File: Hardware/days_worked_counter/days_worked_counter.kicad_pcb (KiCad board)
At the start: 2 copper layers, 96.5 x 50 mm, 29 parts, among them J401 19V Input, SW201 RESET, U201 ATmega328P-A, U301 FT232RL, U401 LM1117-5.0, U501 SN74HC595, U601 SN74HC595, U701 SN74HC595

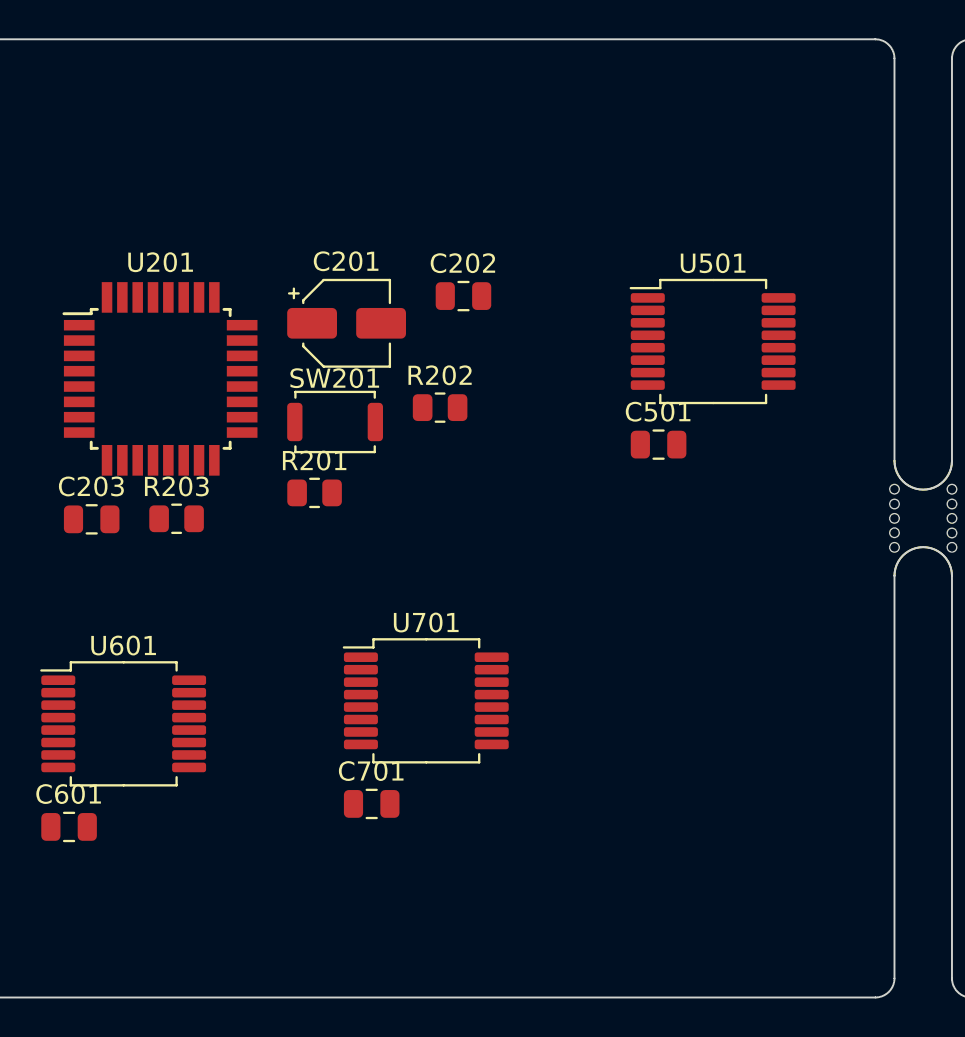
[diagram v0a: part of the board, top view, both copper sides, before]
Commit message: Add tidal force
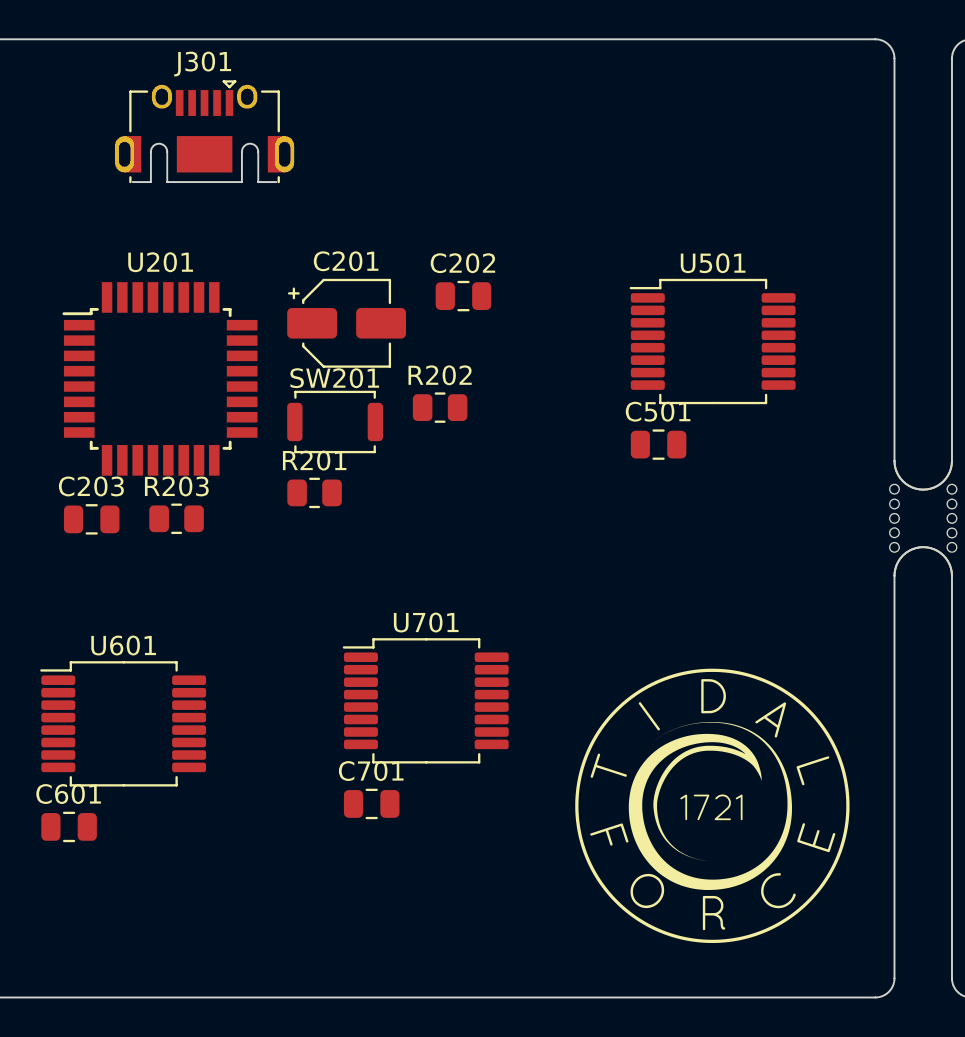
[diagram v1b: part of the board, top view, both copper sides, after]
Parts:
- added G***: LOGO, KenwoodFox:TIDAL_FORCE_LOGO, F.Cu at (188.0, 109.0)
- added J301: USB_B_Micro, Connector_USB:USB_Micro-AB_Molex_47590-0001, F.Cu at (161.5, 75.0)

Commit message: Cleanup more stuff
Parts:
- added Q501: MMBT3904, Package_TO_SOT_SMD:SOT-23, F.Cu at (138.0, 44.0)
- added Q601: MMBT3904, Package_TO_SOT_SMD:SOT-23, F.Cu at (125.6, 52.3)
- added Q701: MMBT3904, Package_TO_SOT_SMD:SOT-23, F.Cu at (125.6, 44.0)
- added R204: 1K, Resistor_SMD:R_0805_2012Metric, F.Cu at (137.8, 51.5)
- added R501: 10K, Resistor_SMD:R_0805_2012Metric, F.Cu at (142.7, 43.2)
- added R601: 10K, Resistor_SMD:R_0805_2012Metric, F.Cu at (130.2, 51.5)
- added R701: 10K, Resistor_SMD:R_0805_2012Metric, F.Cu at (130.2, 43.2)
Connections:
- U201 pad 12: unconnected-(U201-Pad12) -> /Display Card/DATA_IN
- U201 pad 13: unconnected-(U201-Pad13) -> /Display Card/CLOCK_IN
- U201 pad 14: unconnected-(U201-Pad14) -> /Display Card/LATCH_IN
- U201 pad 17: unconnected-(U201-Pad17) -> Net-(U201-Pad17)
- U201 pad 23: unconnected-(U201-Pad23) -> /MCU/DAY_RESET
- U201 pad 24: unconnected-(U201-Pad24) -> /MCU/DAY_ADVANCE
- U201 pad 25: unconnected-(U201-Pad25) -> /MCU/DAY_SUBTRACT
- U501 pad 15: unconnected-(U501-Pad15) -> /Display Card/SEG_A
- U601 pad 15: unconnected-(U601-Pad15) -> /Display Card1/SEG_A
- U701 pad 15: unconnected-(U701-Pad15) -> /Display Card2/SEG_A

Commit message: Add all the cool stuff
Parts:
- added Q502: MMBT3904, Package_TO_SOT_SMD:SOT-23, F.Cu at (191.5, 37.5)
- added Q503: MMBT3904, Package_TO_SOT_SMD:SOT-23, F.Cu at (191.5, 28.6)
- added Q504: MMBT3904, Package_TO_SOT_SMD:SOT-23, F.Cu at (196.4, 28.6)
- added Q505: MMBT3904, Package_TO_SOT_SMD:SOT-23, F.Cu at (186.6, 37.5)
- added Q506: MMBT3904, Package_TO_SOT_SMD:SOT-23, F.Cu at (186.6, 28.6)
- added Q507: MMBT3904, Package_TO_SOT_SMD:SOT-23, F.Cu at (186.6, 33.0)
- added Q508: MMBT3904, Package_TO_SOT_SMD:SOT-23, F.Cu at (191.5, 33.0)
- added Q602: MMBT3904, Package_TO_SOT_SMD:SOT-23, F.Cu at (158.7, 57.3)
- added Q603: MMBT3904, Package_TO_SOT_SMD:SOT-23, F.Cu at (158.7, 48.4)
- added Q604: MMBT3904, Package_TO_SOT_SMD:SOT-23, F.Cu at (163.6, 48.4)
- added Q605: MMBT3904, Package_TO_SOT_SMD:SOT-23, F.Cu at (153.8, 57.3)
- added Q606: MMBT3904, Package_TO_SOT_SMD:SOT-23, F.Cu at (153.8, 48.4)
- added Q607: MMBT3904, Package_TO_SOT_SMD:SOT-23, F.Cu at (153.8, 52.8)
- added Q608: MMBT3904, Package_TO_SOT_SMD:SOT-23, F.Cu at (158.7, 52.8)
- added Q702: MMBT3904, Package_TO_SOT_SMD:SOT-23, F.Cu at (158.7, 37.5)
- added Q703: MMBT3904, Package_TO_SOT_SMD:SOT-23, F.Cu at (158.7, 28.6)
- added Q704: MMBT3904, Package_TO_SOT_SMD:SOT-23, F.Cu at (163.6, 28.6)
- added Q705: MMBT3904, Package_TO_SOT_SMD:SOT-23, F.Cu at (153.8, 37.5)
- added Q706: MMBT3904, Package_TO_SOT_SMD:SOT-23, F.Cu at (153.8, 28.6)
- added Q707: MMBT3904, Package_TO_SOT_SMD:SOT-23, F.Cu at (153.8, 33.0)
- added Q708: MMBT3904, Package_TO_SOT_SMD:SOT-23, F.Cu at (158.7, 33.0)
- added R502: 10K, Resistor_SMD:R_0805_2012Metric, F.Cu at (205.0, 33.8)
- added R503: 10K, Resistor_SMD:R_0805_2012Metric, F.Cu at (200.6, 36.7)
- added R504: 10K, Resistor_SMD:R_0805_2012Metric, F.Cu at (196.2, 32.3)
- added R505: 10K, Resistor_SMD:R_0805_2012Metric, F.Cu at (195.2, 41.2)
- added R506: 750R?, Resistor_SMD:R_0805_2012Metric, F.Cu at (200.6, 33.8)
- added R507: 750R?, Resistor_SMD:R_0805_2012Metric, F.Cu at (205.4, 27.9)
- added R508: 750R?, Resistor_SMD:R_0805_2012Metric, F.Cu at (196.2, 35.2)
- added R509: 750R?, Resistor_SMD:R_0805_2012Metric, F.Cu at (205.4, 30.8)
- added R510: 10K, Resistor_SMD:R_0805_2012Metric, F.Cu at (201.0, 27.9)
- added R511: 10K, Resistor_SMD:R_0805_2012Metric, F.Cu at (190.8, 41.2)
- added R512: 10K, Resistor_SMD:R_0805_2012Metric, F.Cu at (199.6, 41.1)
- added R513: 750R?, Resistor_SMD:R_0805_2012Metric, F.Cu at (196.2, 38.2)
- added R514: 750R?, Resistor_SMD:R_0805_2012Metric, F.Cu at (209.9, 27.9)
- added R515: 750R?, Resistor_SMD:R_0805_2012Metric, F.Cu at (186.4, 41.2)
- added R516: 750R?, Resistor_SMD:R_0805_2012Metric, F.Cu at (201.0, 30.8)
- added R602: 10K, Resistor_SMD:R_0805_2012Metric, F.Cu at (172.2, 53.5)
- added R603: 10K, Resistor_SMD:R_0805_2012Metric, F.Cu at (167.7, 56.5)
- added R604: 10K, Resistor_SMD:R_0805_2012Metric, F.Cu at (163.3, 52.1)
- added R605: 10K, Resistor_SMD:R_0805_2012Metric, F.Cu at (162.4, 61.0)
- added R606: 750R?, Resistor_SMD:R_0805_2012Metric, F.Cu at (167.7, 53.5)
- added R607: 750R?, Resistor_SMD:R_0805_2012Metric, F.Cu at (172.6, 47.6)
- added R608: 750R?, Resistor_SMD:R_0805_2012Metric, F.Cu at (163.3, 55.0)
- added R609: 750R?, Resistor_SMD:R_0805_2012Metric, F.Cu at (172.6, 50.6)
- added R610: 10K, Resistor_SMD:R_0805_2012Metric, F.Cu at (168.2, 47.6)
- added R611: 10K, Resistor_SMD:R_0805_2012Metric, F.Cu at (158.0, 61.0)
- added R612: 10K, Resistor_SMD:R_0805_2012Metric, F.Cu at (166.8, 60.9)
- added R613: 750R?, Resistor_SMD:R_0805_2012Metric, F.Cu at (163.3, 58.0)
- added R614: 750R?, Resistor_SMD:R_0805_2012Metric, F.Cu at (177.0, 47.6)
- added R615: 750R?, Resistor_SMD:R_0805_2012Metric, F.Cu at (153.6, 61.0)
- added R616: 750R?, Resistor_SMD:R_0805_2012Metric, F.Cu at (168.2, 50.6)
- added R702: 10K, Resistor_SMD:R_0805_2012Metric, F.Cu at (172.2, 33.8)
- added R703: 10K, Resistor_SMD:R_0805_2012Metric, F.Cu at (167.7, 36.7)
- added R704: 10K, Resistor_SMD:R_0805_2012Metric, F.Cu at (163.3, 32.3)
- added R705: 10K, Resistor_SMD:R_0805_2012Metric, F.Cu at (162.4, 41.2)
- added R706: 750R?, Resistor_SMD:R_0805_2012Metric, F.Cu at (167.7, 33.8)
- added R707: 750R?, Resistor_SMD:R_0805_2012Metric, F.Cu at (172.6, 27.9)
- added R708: 750R?, Resistor_SMD:R_0805_2012Metric, F.Cu at (163.3, 35.2)
- added R709: 750R?, Resistor_SMD:R_0805_2012Metric, F.Cu at (172.6, 30.8)
- added R710: 10K, Resistor_SMD:R_0805_2012Metric, F.Cu at (168.2, 27.9)
- added R711: 10K, Resistor_SMD:R_0805_2012Metric, F.Cu at (158.0, 41.2)
- added R712: 10K, Resistor_SMD:R_0805_2012Metric, F.Cu at (166.8, 41.1)
- added R713: 750R?, Resistor_SMD:R_0805_2012Metric, F.Cu at (163.3, 38.2)
- added R714: 750R?, Resistor_SMD:R_0805_2012Metric, F.Cu at (177.0, 27.9)
- added R715: 750R?, Resistor_SMD:R_0805_2012Metric, F.Cu at (153.6, 41.2)
- added R716: 750R?, Resistor_SMD:R_0805_2012Metric, F.Cu at (168.2, 30.8)
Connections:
- net /Display Card/CLOCK_IN renamed /Display Card 0/CLOCK_IN
- net /Display Card/DATA_IN renamed /Display Card 0/DATA_IN
- net /Display Card/DATA_OUT renamed /Display Card 0/DATA_OUT
- net /Display Card/LATCH_IN renamed /Display Card 0/LATCH_IN
- net /Display Card1/DATA_OUT renamed /Display Card 1/DATA_OUT
- net /Display Card2/DATA_OUT renamed /Display Card 2/DATA_OUT
- Q501 pad 1: /Display Card/SEG_A -> /Display Card 0/SEG_B
- Q501 pad 3: /Display Card/SEG_A_LAMP -> Net-(Q501-Pad3)
- Q601 pad 1: /Display Card1/SEG_A -> /Display Card 1/SEG_B
- Q601 pad 3: /Display Card1/SEG_A_LAMP -> Net-(Q601-Pad3)
- Q701 pad 1: /Display Card2/SEG_A -> /Display Card 2/SEG_B
- Q701 pad 3: /Display Card2/SEG_A_LAMP -> Net-(Q701-Pad3)
- R501 pad 1: /Display Card/SEG_A -> /Display Card 0/SEG_B
- R601 pad 1: /Display Card1/SEG_A -> /Display Card 1/SEG_B
- R701 pad 1: /Display Card2/SEG_A -> /Display Card 2/SEG_B
- U501 pad 1: unconnected-(U501-Pad1) -> /Display Card 0/SEG_B
- U501 pad 15: /Display Card/SEG_A -> /Display Card 0/SEG_A
- U501 pad 2: unconnected-(U501-Pad2) -> /Display Card 0/SEG_C
- U501 pad 3: unconnected-(U501-Pad3) -> /Display Card 0/SEG_D
- U501 pad 4: unconnected-(U501-Pad4) -> /Display Card 0/SEG_E
- U501 pad 5: unconnected-(U501-Pad5) -> /Display Card 0/SEG_F
- U501 pad 6: unconnected-(U501-Pad6) -> /Display Card 0/SEG_G
- U501 pad 7: unconnected-(U501-Pad7) -> /Display Card 0/SEG_H
- U601 pad 1: unconnected-(U601-Pad1) -> /Display Card 1/SEG_B
- U601 pad 15: /Display Card1/SEG_A -> /Display Card 1/SEG_A
- U601 pad 2: unconnected-(U601-Pad2) -> /Display Card 1/SEG_C
- U601 pad 3: unconnected-(U601-Pad3) -> /Display Card 1/SEG_D
- U601 pad 4: unconnected-(U601-Pad4) -> /Display Card 1/SEG_E
- U601 pad 5: unconnected-(U601-Pad5) -> /Display Card 1/SEG_F
- U601 pad 6: unconnected-(U601-Pad6) -> /Display Card 1/SEG_G
- U601 pad 7: unconnected-(U601-Pad7) -> /Display Card 1/SEG_H
- U701 pad 1: unconnected-(U701-Pad1) -> /Display Card 2/SEG_B
- U701 pad 15: /Display Card2/SEG_A -> /Display Card 2/SEG_A
- U701 pad 2: unconnected-(U701-Pad2) -> /Display Card 2/SEG_C
- U701 pad 3: unconnected-(U701-Pad3) -> /Display Card 2/SEG_D
- U701 pad 4: unconnected-(U701-Pad4) -> /Display Card 2/SEG_E
- U701 pad 5: unconnected-(U701-Pad5) -> /Display Card 2/SEG_F
- U701 pad 6: unconnected-(U701-Pad6) -> /Display Card 2/SEG_G
- U701 pad 7: unconnected-(U701-Pad7) -> /Display Card 2/SEG_H

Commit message: Even more stuff
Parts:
- added BT201: 3v, Battery:BatteryHolder_Keystone_3034_1x20mm, F.Cu at (242.6, 114.6)
- added D201: STAT, LED_SMD:LED_0805_2012Metric, F.Cu at (215.0, 71.6)
- added J302: PROG, Connector_PinSocket_2.54mm:PinSocket_1x06_P2.54mm_Vertical, F.Cu at (88.7, 80.2)
- added J501: Conn_01x09, Connector_PinSocket_2.54mm:PinSocket_1x09_P2.54mm_Vertical, F.Cu at (269.6, 40.7)
- added J502: Conn_01x09, Connector_PinSocket_2.54mm:PinSocket_1x09_P2.54mm_Vertical, F.Cu at (274.2, 40.7)
- added J601: Conn_01x09, Connector_PinSocket_2.54mm:PinSocket_1x09_P2.54mm_Vertical, F.Cu at (242.3, 40.7)
- added J602: Conn_01x09, Connector_PinSocket_2.54mm:PinSocket_1x09_P2.54mm_Vertical, F.Cu at (246.9, 40.7)
- added J701: Conn_01x09, Connector_PinSocket_2.54mm:PinSocket_1x09_P2.54mm_Vertical, F.Cu at (215.1, 40.7)
- added J702: Conn_01x09, Connector_PinSocket_2.54mm:PinSocket_1x09_P2.54mm_Vertical, F.Cu at (219.7, 40.7)
- added JP301: SolderJumper_2_Open, Jumper:SolderJumper-2_P1.3mm_Open_TrianglePad1.0x1.5mm, F.Cu at (92.7, 87.8)
- added R205: 10K, Resistor_SMD:R_0805_2012Metric, F.Cu at (232.4, 127.1)
- added R206: 10K, Resistor_SMD:R_0805_2012Metric, F.Cu at (257.2, 111.5)
- added U202: DS1307Z+, Package_SO:SOIC-8_3.9x4.9mm_P1.27mm, F.Cu at (259.2, 106.8)
- J301: footprint Connector_USB:USB_Micro-AB_Molex_47590-0001 -> Connector_USB:USB_Mini-B_Lumberg_2486_01_Horizontal
- moved J301 84.0 mm to (77.6, 71.2), turned to 180 degrees
- moved R302 72.5 mm to (73.0, 98.0)
- moved D302 69.6 mm to (76.6, 98.0)
- moved D301 64.1 mm to (76.8, 94.0)
- moved U401 63.7 mm to (75.8, 120.6)
- moved R301 62.8 mm to (73.0, 94.0)
- moved D401 61.9 mm to (85.7, 121.2)
- moved C401 60.8 mm to (75.8, 125.4)
- moved J401 60.2 mm to (72.2, 130.2)
- moved C303 55.5 mm to (79.2, 77.2), turned to -90 degrees
- moved C301 53.4 mm to (70.2, 83.4), turned to -90 degrees
- moved R401 53.1 mm to (82.2, 121.2)
- moved C302 53.0 mm to (83.6, 77.6)
- moved U301 49.3 mm to (76.2, 85.4), turned to 180 degrees
- moved C304 43.1 mm to (84.2, 89.0), turned to 180 degrees
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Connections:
- U201 pad 27: unconnected-(U201-Pad27) -> /MCU/SDA
- U201 pad 28: unconnected-(U201-Pad28) -> /MCU/SCL

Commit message: get input from @ka2qfx
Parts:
- removed Q502, Q503, Q504, Q505, Q506, Q507, Q508, Q602, Q603, Q604, Q605, Q606, Q607, Q608, Q702, Q703, Q704, Q705, Q706, Q707, Q708: MMBT3904, Package_TO_SOT_SMD:SOT-23
- removed R502, R503, R504, R505, R510, R511, R512, R602, R603, R604, R605, R610, R611, R612, R702, R703, R704, R705, R710, R711, R712: 10K, Resistor_SMD:R_0805_2012Metric
- removed R506, R507, R508, R509, R513, R514, R515, R516, R606, R607, R608, R609, R613, R614, R615, R616, R706, R707, R708, R709, R713, R714, R715, R716: 750R?, Resistor_SMD:R_0805_2012Metric
- removed the mouse-bite-3mm-slot at (199.0, 94.0)
- added C204: 22pf, Capacitor_SMD:C_0805_2012Metric, F.Cu at (320.0, -7.20)
- added C205: 22pf, Capacitor_SMD:C_0805_2012Metric, F.Cu at (320.0, -10.2)
- added J101: OUT, Connector_PinSocket_2.54mm:PinSocket_1x06_P2.54mm_Vertical, F.Cu at (83.5, 127.2)
- added J102: IN, Connector_PinSocket_2.54mm:PinSocket_1x06_P2.54mm_Vertical, F.Cu at (91.5, 127.2)
- added J103: OUT, Connector_PinSocket_2.54mm:PinSocket_1x06_P2.54mm_Vertical, F.Cu at (118.5, 127.2)
- added J104: IN, Connector_PinSocket_2.54mm:PinSocket_1x06_P2.54mm_Vertical, F.Cu at (126.5, 127.2)
- added J105: OUT, Connector_PinSocket_2.54mm:PinSocket_1x06_P2.54mm_Vertical, F.Cu at (153.0, 127.2)
- added R207: 10K, Resistor_SMD:R_0805_2012Metric, F.Cu at (279.4, -17.8)
- added R208: 10K, Resistor_SMD:R_0805_2012Metric, F.Cu at (279.4, -20.8)
- added R209: 10K, Resistor_SMD:R_0805_2012Metric, F.Cu at (289.9, -29.3)
- added SW202: DAY_RESET, Button_Switch_THT:SW_PUSH_6mm_H5mm, F.Cu at (279.2, -28.8)
- added SW203: DAY_ADV, Button_Switch_THT:SW_PUSH_6mm_H5mm, F.Cu at (268.7, -28.8)
- added SW204: DAY_SUB, Button_Switch_THT:SW_PUSH_6mm_H5mm, F.Cu at (268.7, -20.2)
- added Y201: 16mHz, Crystal:Crystal_SMD_HC49-SD, F.Cu at (310.4, -8.59)
- added Y202: 32.768kHz, Crystal:Crystal_SMD_HC49-SD, F.Cu at (310.4, -2.34)
- added mouse-bite-3mm-slot: VAL**, Panelization:mouse-bite-3mm-slot, F.Cu at (122.5, 42.5)
- added mouse-bite-3mm-slot: VAL**, Panelization:mouse-bite-3mm-slot, F.Cu at (122.5, 147.5)
- added mouse-bite-3mm-slot: VAL**, Panelization:mouse-bite-3mm-slot, F.Cu at (87.5, 42.5)
- added mouse-bite-3mm-slot: VAL**, Panelization:mouse-bite-3mm-slot, F.Cu at (87.5, 147.5)
- J501, J601, J701: value Conn_01x09 -> Top Conn; moved to B.Cu
- J502, J602, J702: value Conn_01x09 -> Bottom Conn; moved to B.Cu
- SW201: footprint Button_Switch_SMD:SW_Push_SPST_NO_Alps_SKRK -> Button_Switch_THT:SW_PUSH_6mm_H5mm
- moved C301 272.4 mm to (266.2, -105.8)
- moved C302 272.4 mm to (279.6, -111.6)
- moved C303 272.4 mm to (275.2, -112.0)
- moved C304 272.4 mm to (280.2, -100.2)
- moved D301 272.4 mm to (272.8, -95.2)
- moved D302 272.4 mm to (272.6, -91.2)
- moved J301 272.4 mm to (273.6, -118.0)
- moved J302 272.4 mm to (284.7, -109.0)
- moved JP301 272.4 mm to (288.7, -101.4)
- moved Q501 272.4 mm to (334.0, -145.2)
- moved Q601 272.4 mm to (321.6, -136.9)
- moved Q701 272.4 mm to (321.6, -145.2)
- moved R204 272.4 mm to (333.8, -137.7)
- moved R301 272.4 mm to (269.0, -95.2)
- moved R302 272.4 mm to (269.0, -91.2)
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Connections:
- net Net-(J401-Pad1) renamed +19V
- J501 pad 1: /Display Card 0/SEG_E_LAMP -> /Display Card 0/SEG_B_LAMP
- J501 pad 3: /Display Card 0/SEG_F_LAMP -> /Display Card 0/SEG_A_LAMP
- J501 pad 5: /Display Card 0/SEG_G_LAMP -> unconnected-(J501-Pad5)
- J501 pad 7: /Display Card 0/SEG_H_LAMP -> /Display Card 0/SEG_F_LAMP
- J501 pad 9: GND -> /Display Card 0/SEG_G_LAMP
- J502 pad 1: +12V -> /Display Card 0/SEG_H_LAMP
- J502 pad 3: /Display Card 0/SEG_A_LAMP -> /Display Card 0/SEG_C_LAMP
- J502 pad 5: /Display Card 0/SEG_B_LAMP -> /Display Card 0/SEG_D_LAMP
- J502 pad 7: /Display Card 0/SEG_C_LAMP -> /Display Card 0/SEG_E_LAMP
- J502 pad 9: /Display Card 0/SEG_D_LAMP -> GND
- J601 pad 1: /Display Card 1/SEG_E_LAMP -> /Display Card 1/SEG_B_LAMP
- J601 pad 3: /Display Card 1/SEG_F_LAMP -> /Display Card 1/SEG_A_LAMP
- J601 pad 5: /Display Card 1/SEG_G_LAMP -> unconnected-(J601-Pad5)
- J601 pad 7: /Display Card 1/SEG_H_LAMP -> /Display Card 1/SEG_F_LAMP
- J601 pad 9: GND -> /Display Card 1/SEG_G_LAMP
- J602 pad 1: +12V -> /Display Card 1/SEG_H_LAMP
- J602 pad 3: /Display Card 1/SEG_A_LAMP -> /Display Card 1/SEG_C_LAMP
- J602 pad 5: /Display Card 1/SEG_B_LAMP -> /Display Card 1/SEG_D_LAMP
- J602 pad 7: /Display Card 1/SEG_C_LAMP -> /Display Card 1/SEG_E_LAMP
- J602 pad 9: /Display Card 1/SEG_D_LAMP -> GND
- J701 pad 1: /Display Card 2/SEG_E_LAMP -> /Display Card 2/SEG_B_LAMP
- J701 pad 3: /Display Card 2/SEG_F_LAMP -> /Display Card 2/SEG_A_LAMP
- J701 pad 5: /Display Card 2/SEG_G_LAMP -> unconnected-(J701-Pad5)
- J701 pad 7: /Display Card 2/SEG_H_LAMP -> /Display Card 2/SEG_F_LAMP
- J701 pad 9: GND -> /Display Card 2/SEG_G_LAMP
- J702 pad 1: +12V -> /Display Card 2/SEG_H_LAMP
- J702 pad 3: /Display Card 2/SEG_A_LAMP -> /Display Card 2/SEG_C_LAMP
- J702 pad 5: /Display Card 2/SEG_B_LAMP -> /Display Card 2/SEG_D_LAMP
- J702 pad 7: /Display Card 2/SEG_C_LAMP -> /Display Card 2/SEG_E_LAMP
- J702 pad 9: /Display Card 2/SEG_D_LAMP -> GND
- U201 pad 1: unconnected-(U201-Pad1) -> /MCU/DAY_ADVANCE
- U201 pad 2: unconnected-(U201-Pad2) -> /MCU/DAY_SUBTRACT
- U201 pad 23: /MCU/DAY_RESET -> unconnected-(U201-Pad23)
- U201 pad 24: /MCU/DAY_ADVANCE -> unconnected-(U201-Pad24)
- U201 pad 25: /MCU/DAY_SUBTRACT -> unconnected-(U201-Pad25)
- U201 pad 32: unconnected-(U201-Pad32) -> /MCU/DAY_RESET
- U601 pad 11: /Display Card 0/CLOCK_IN -> /Display Card 1/CLOCK_IN
- U601 pad 12: /Display Card 0/LATCH_IN -> /Display Card 1/LATCH_IN
- U601 pad 14: /Display Card 0/DATA_OUT -> /Display Card 1/DATA_IN
- U701 pad 11: /Display Card 0/CLOCK_IN -> /Display Card 2/CLOCK_IN
- U701 pad 12: /Display Card 0/LATCH_IN -> /Display Card 2/LATCH_IN
- U701 pad 14: /Display Card 1/DATA_OUT -> /Display Card 2/DATA_IN
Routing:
- added copper zone on B.Cu, net GND
- added copper zone on F.Cu, net GND
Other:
- board size 96.5 x 50 mm -> 114.5 x 141 mm
- board text added: "A"
- board text added: "B"
- board text added: "C"
- board text added: "D"
- board text added: "DP"
- board text added: "E"
- board text added: "F"
- board text added: "G"
- board text added: "GND"
